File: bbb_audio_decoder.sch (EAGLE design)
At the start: 183 parts, among them IC1 OPA2134, IC2 LM317, IC3 LM337, IC4 OPA2134, IC5 OPA2134, IC6 OPA2134, P1 PLR135/T9, P9 P9, Q1 BS170, Q2 BS170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

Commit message: Made gebers of ver1
(and snuck in a component value change, because it was a bug and is still
part of ver1)
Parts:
- R10, R11: value 68 -> 120
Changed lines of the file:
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@@
 <part name="Q1" library="transistor-small-signal" deviceset="BS170" device=""/>
 <part name="SUPPLY52" library="supply2" deviceset="DGND" device=""/>
-<part name="R10" library="rcl" deviceset="R-EU_" device="0204/2V" value="68"/>
+<part name="R10" library="rcl" deviceset="R-EU_" device="0204/2V" value="120"/>
 <part name="SUPPLY53" library="supply2" deviceset="VDD" device=""/>
 <part name="Q2" library="transistor-small-signal" deviceset="BS170" device=""/>
 <part name="SUPPLY54" library="supply2" deviceset="DGND" device=""/>
-<part name="R11" library="rcl" deviceset="R-EU_" device="0204/2V" value="68"/>
+<part name="R11" library="rcl" deviceset="R-EU_" device="0204/2V" value="120"/>
 <part name="SUPPLY55" library="supply2" deviceset="VDD" device=""/>
 <part name="READY" library="con-molex" deviceset="22-23-2021" device=""/>

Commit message: Renamed 5.5 mm adapter symbol
This one specifies the inner diameter too.
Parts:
- AC: value ADAPTER-PLUG-5.5MM -> ADAPTER-PLUG-5.5/2.1MM; device 0000halfgaar:ADAPTER-PLUG-5.5MM -> 0000halfgaar:ADAPTER-PLUG-5.5/2.1MM
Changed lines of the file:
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@@
 <part name="P-1" library="supply1" deviceset="V-" device=""/>
 <part name="C32" library="rcl" deviceset="C-EU" device="050-024X044" value="100nf"/>
-<part name="AC" library="0000halfgaar" deviceset="ADAPTER-PLUG-5.5MM" device=""/>
 <part name="C33" library="rcl" deviceset="CPOL-EU" device="E2.5-6" value="22µF/25V"/>
 <part name="C34" library="rcl" deviceset="CPOL-EU" device="E2.5-6" value="22µF/25V"/>
@@
 <part name="C17" library="rcl" deviceset="CPOL-EU" device="E2-5" value="10 µF"/>
 <part name="SUPPLY24" library="supply2" deviceset="DGND" device=""/>
+<part name="AC" library="0000halfgaar" deviceset="ADAPTER-PLUG-5.5/2.1MM" device=""/>
 </parts>
 <sheets>
@@
 <instance part="P-1" gate="1" x="109.22" y="167.64"/>
 <instance part="C32" gate="G$1" x="137.16" y="215.9"/>
-<instance part="AC" gate="1" x="7.62" y="223.52"/>
-<instance part="AC" gate="2" x="7.62" y="215.9"/>
 <instance part="C33" gate="G$1" x="55.88" y="205.74"/>
 <instance part="C34" gate="G$1" x="55.88" y="228.6"/>
@@
 <instance part="C17" gate="G$1" x="-91.44" y="73.66"/>
 <instance part="SUPPLY24" gate="G$1" x="-91.44" y="60.96"/>
+<instance part="AC" gate="1" x="7.62" y="223.52"/>
+<instance part="AC" gate="2" x="7.62" y="215.9"/>
 </instances>
 <busses>
@@
 <pinref part="C24" gate="G$1" pin="-"/>
 <pinref part="C25" gate="G$1" pin="+"/>
-<pinref part="AC" gate="2" pin="KL"/>
 <pinref part="C33" gate="G$1" pin="+"/>
 <wire x1="55.88" y1="208.28" x2="55.88" y2="215.9" width="0.1524" layer="91"/>
@@
 <wire x1="116.84" y1="215.9" x2="114.3" y2="215.9" width="0.1524" layer="91"/>
 <junction x="114.3" y="215.9"/>
-</segment>
-<segment>
+<pinref part="AC" gate="2" pin="KL"/>
+</segment>
+<segment>

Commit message: Use updated PCM1690 package
Description was wrong, and the thermal pad wasn't connected.
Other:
- moved on the sheet: U1

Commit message: Fixes wrong net name
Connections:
- net AHCLKX renamed FSX
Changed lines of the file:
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@@
 </segment>
 </net>
-<net name="AHCLKX" class="0">
+<net name="FSX" class="0">
 <segment>
 <pinref part="P9" gate="G$1" pin="FSX"/>

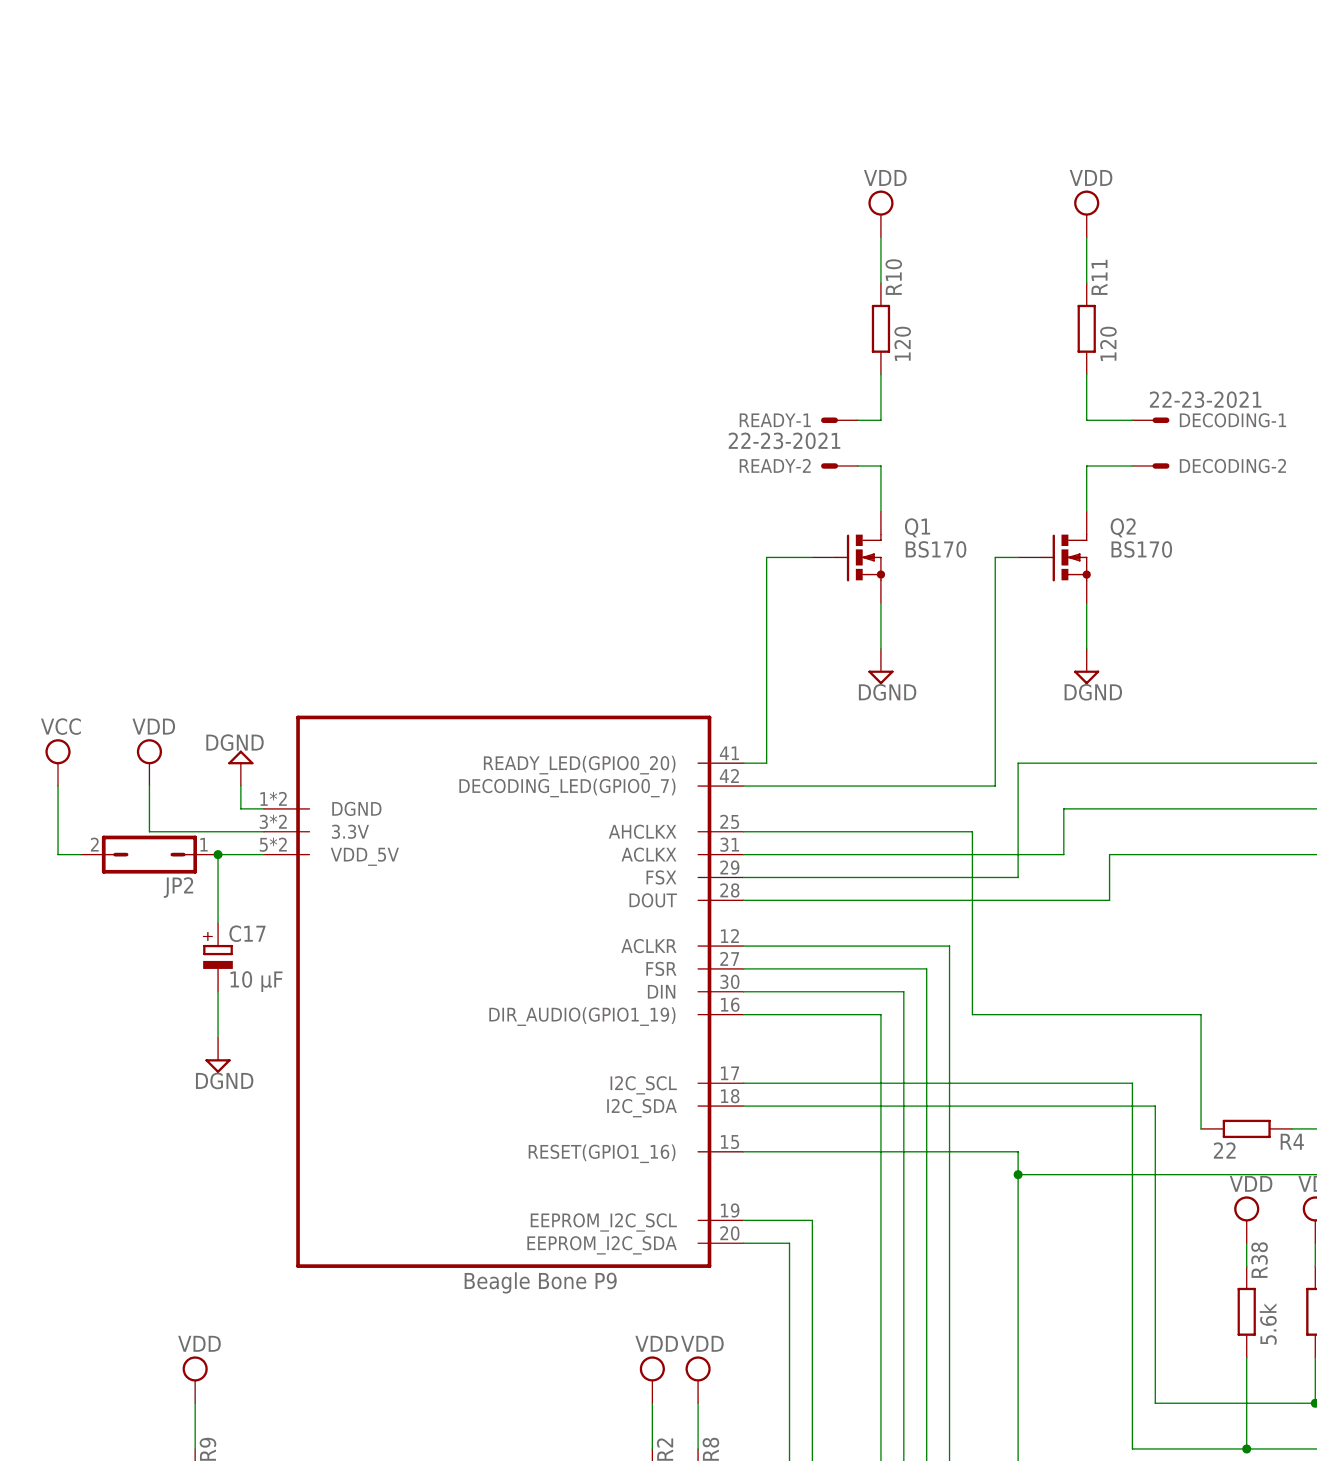
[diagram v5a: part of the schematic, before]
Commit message: Use P9 connector with wiring for slave m-clock
As described from the eaglecustom repo:

> For my purpose, I need to use an external master clock. This is input on
> ahclkr, which is pin 28. For that, the previous pin 28 function, axr2,
> has been moved to axr1, pin 41. And for that, the 'ready' LED that was
> on pin 41 has been removed.
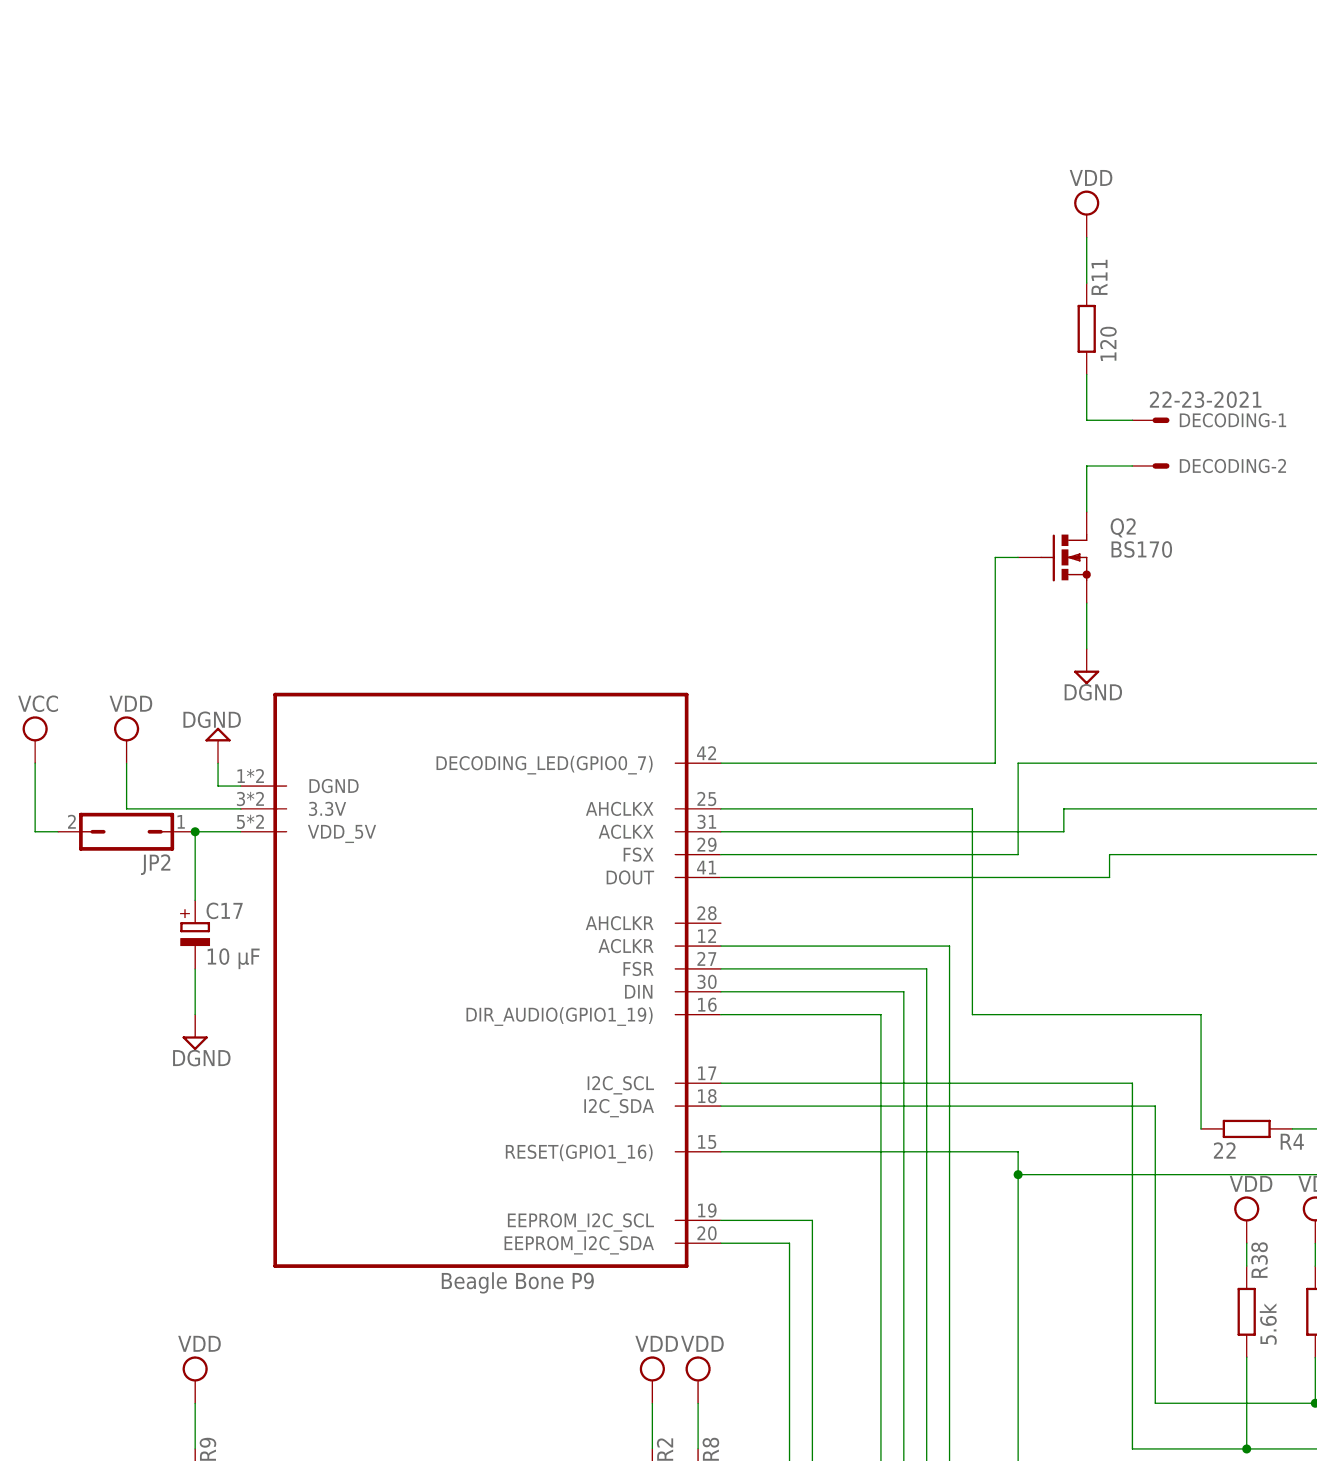
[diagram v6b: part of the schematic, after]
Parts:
- removed P9: P9, 0000halfgaar:BEAGLEBONEP9
- removed Q1: BS170, transistor-small-signal:BS170
- removed R10: 120, rcl:R-EU_0204/2V
- removed READY: 22-23-2021, con-molex:22-23-2021
- added U$1: BEAGLEBONEP9, 0000halfgaar:BEAGLEBONEP9
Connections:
- removed net N$28: R10.1, READY-1.S
- removed net N$4: Q1.D, READY-2.S
- removed net N$93: P9.READY_LED(GPIO0_20), Q1.G
- net ACLKR: now also U$1.ACLKR; no longer P9.ACLKR
- net ACLKX: now also U$1.ACLKX; no longer P9.ACLKX
- net CAPE_I2C_SCL: now also U$1.EEPROM_I2C_SCL; no longer P9.EEPROM_I2C_SCL
- net CAPE_I2C_SDA: now also U$1.EEPROM_I2C_SDA; no longer P9.EEPROM_I2C_SDA
- net DGND: now also U$1.DGND; no longer P9.DGND, Q1.S
- net DIN: now also U$1.DIN; no longer P9.DIN
- net DIR_AUDIO: now also U$1.DIR_AUDIO(GPIO1_19); no longer P9.DIR_AUDIO(GPIO1_19)
- net DOUT: now also U$1.DOUT; no longer P9.DOUT
- net FSR: now also U$1.FSR; no longer P9.FSR
- net FSX: now also U$1.FSX; no longer P9.FSX
- net MCLK: now also U$1.AHCLKX; no longer P9.AHCLKX
- net N$94: now also U$1.DECODING_LED(GPIO0_7); no longer P9.DECODING_LED(GPIO0_7)
- net RST: now also U$1.RESET(GPIO1_16); no longer P9.RESET(GPIO1_16)
- net SCL: now also U$1.I2C_SCL; no longer P9.I2C_SCL
- net SDA: now also U$1.I2C_SDA; no longer P9.I2C_SDA
- net VDD: now also U$1.3.3V; no longer P9.3.3V, R10.2
- net VDD_5V: now also U$1.VDD_5V; no longer P9.VDD_5V
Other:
- moved on the sheet: C17, JP2

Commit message: Set DIR9001 SCKO to 512 * Fs
Both PSCKO pins connect to VDD. I need this to drive 8 channel TDM mode
in the mcasp in the Beagle Bone.
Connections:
- net VDD: now also U2.PSCK0, U2.PSCK1
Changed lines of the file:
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@@
 <part name="AC" library="0000halfgaar" deviceset="ADAPTER-PLUG-5.5/2.1MM" device=""/>
 <part name="U$1" library="0000halfgaar" deviceset="BEAGLEBONEP9" device=""/>
+<part name="SUPPLY26" library="supply2" deviceset="VDD" device=""/>
 </parts>
 <sheets>
@@
 <instance part="AC" gate="2" x="7.62" y="215.9"/>
 <instance part="U$1" gate="G$1" x="-60.96" y="58.42"/>
+<instance part="SUPPLY26" gate="G$1" x="78.74" y="-134.62" rot="R180"/>
 </instances>
 <busses>
@@
 <wire x1="-101.6" y1="88.9" x2="-88.9" y2="88.9" width="0.1524" layer="91"/>
 </segment>
+<segment>
+<pinref part="U2" gate="G$1" pin="PSCK1"/>
+<pinref part="SUPPLY26" gate="G$1" pin="VDD"/>
+<wire x1="83.82" y1="-129.54" x2="78.74" y2="-129.54" width="0.1524" layer="91"/>
+<wire x1="78.74" y1="-129.54" x2="78.74" y2="-132.08" width="0.1524" layer="91"/>
+<pinref part="U2" gate="G$1" pin="PSCK0"/>
+<wire x1="83.82" y1="-124.46" x2="78.74" y2="-124.46" width="0.1524" layer="91"/>
+<wire x1="78.74" y1="-124.46" x2="78.74" y2="-129.54" width="0.1524" layer="91"/>
+<junction x="78.74" y="-129.54"/>
+</segment>
 </net>

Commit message: DIR9001 SCKO goes to input of PCM1690 and BBB
This follows commit c6b4b11003516838945a68f4a9d2063d0b8848d0; we now
actually connect the master clock.
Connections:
- net N$5: now also U2.SCKO
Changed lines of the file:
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@@
 <pinref part="R4" gate="G$1" pin="2"/>
 <pinref part="U1" gate="U$1" pin="SCKI"/>
-<wire x1="27.94" y1="53.34" x2="76.2" y2="53.34" width="0.1524" layer="91"/>
+<wire x1="27.94" y1="53.34" x2="38.1" y2="53.34" width="0.1524" layer="91"/>
+<wire x1="38.1" y1="53.34" x2="76.2" y2="53.34" width="0.1524" layer="91"/>
+<wire x1="38.1" y1="53.34" x2="38.1" y2="-71.12" width="0.1524" layer="91"/>
+<junction x="38.1" y="53.34"/>
+<wire x1="38.1" y1="-71.12" x2="73.66" y2="-71.12" width="0.1524" layer="91"/>
+<wire x1="73.66" y1="-71.12" x2="73.66" y2="-78.74" width="0.1524" layer="91"/>
+<pinref part="U2" gate="G$1" pin="SCKO"/>
+<wire x1="73.66" y1="-78.74" x2="83.82" y2="-78.74" width="0.1524" layer="91"/>
 </segment>
 </net>
